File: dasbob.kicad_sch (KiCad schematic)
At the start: 68 parts, among them J1 TRRS LEFT, J2 TRRS LEFT, SW1 SW_Push, SW10 SW_Push, SW11 SW_Push, SW12 SW_Push, SW13 SW_Push, SW14 SW_Push, SW15 SW_Push, SW16 SW_Push, SW17 SW_Push, SW18 SW_Push, SW19 SW_Push, SW2 SW_Push, SW20 SW_Push, SW21 SW_Push, SW22 SW_Push, SW23 SW_Push, SW24 SW_Push, SW25 SW_Push, SW26 SW_Push, SW27 SW_Push, SW28 SW_Push, SW29 SW_Push, SW3 SW_Push, SW30 SW_Push, SW31 SW_Push, SW32 SW_Push, SW33 SW_Push, SW34 SW_Push, SW35 SW_Push, SW36 SW_Push, SW4 SW_Push, SW5 SW_Push, SW6 SW_Push, SW7 SW_Push, SW8 SW_Push, SW9 SW_Push, U1 Elite-C RIGHT, U2 Elite-C LEFT, U3 OLED1, U4 OLED2

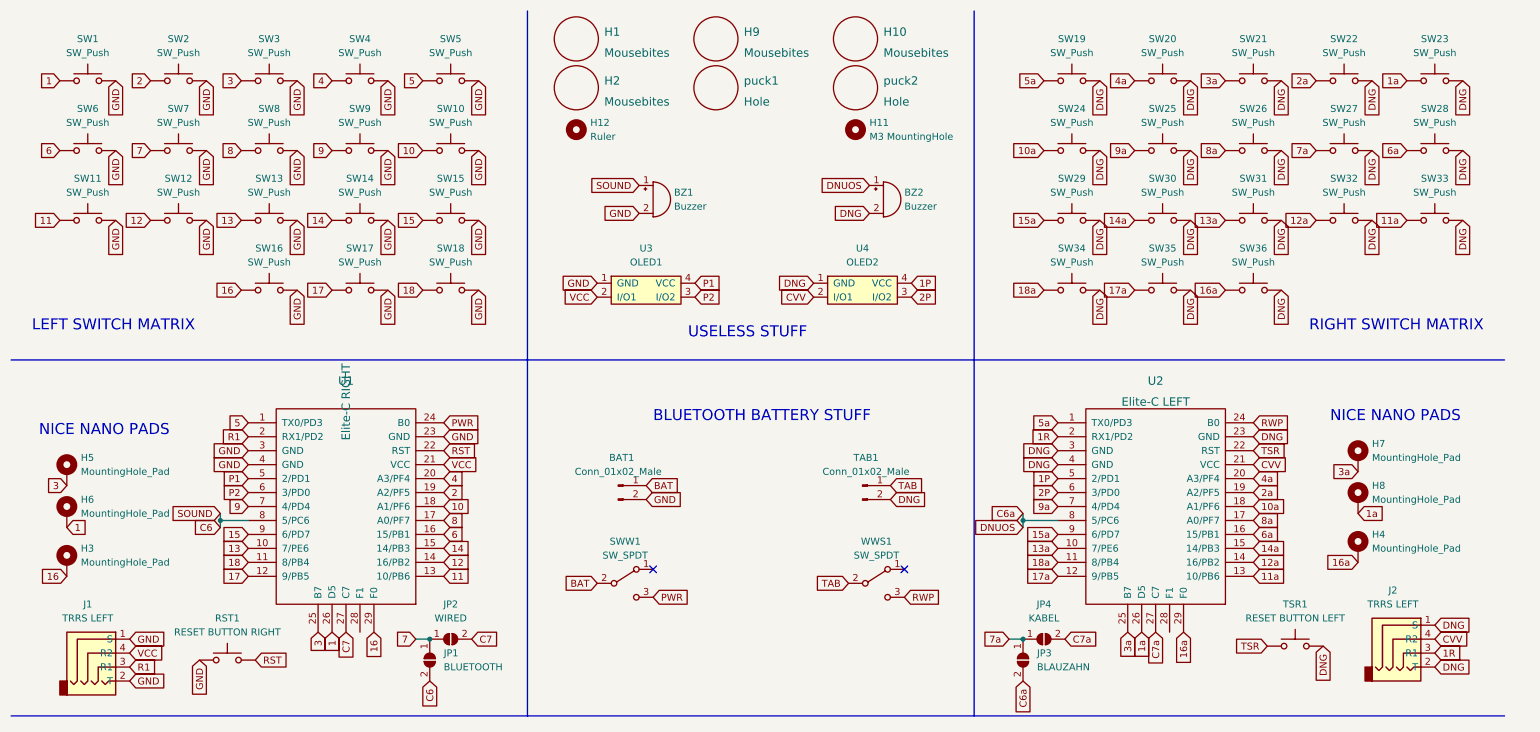
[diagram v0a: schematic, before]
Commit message: Remove jumpers
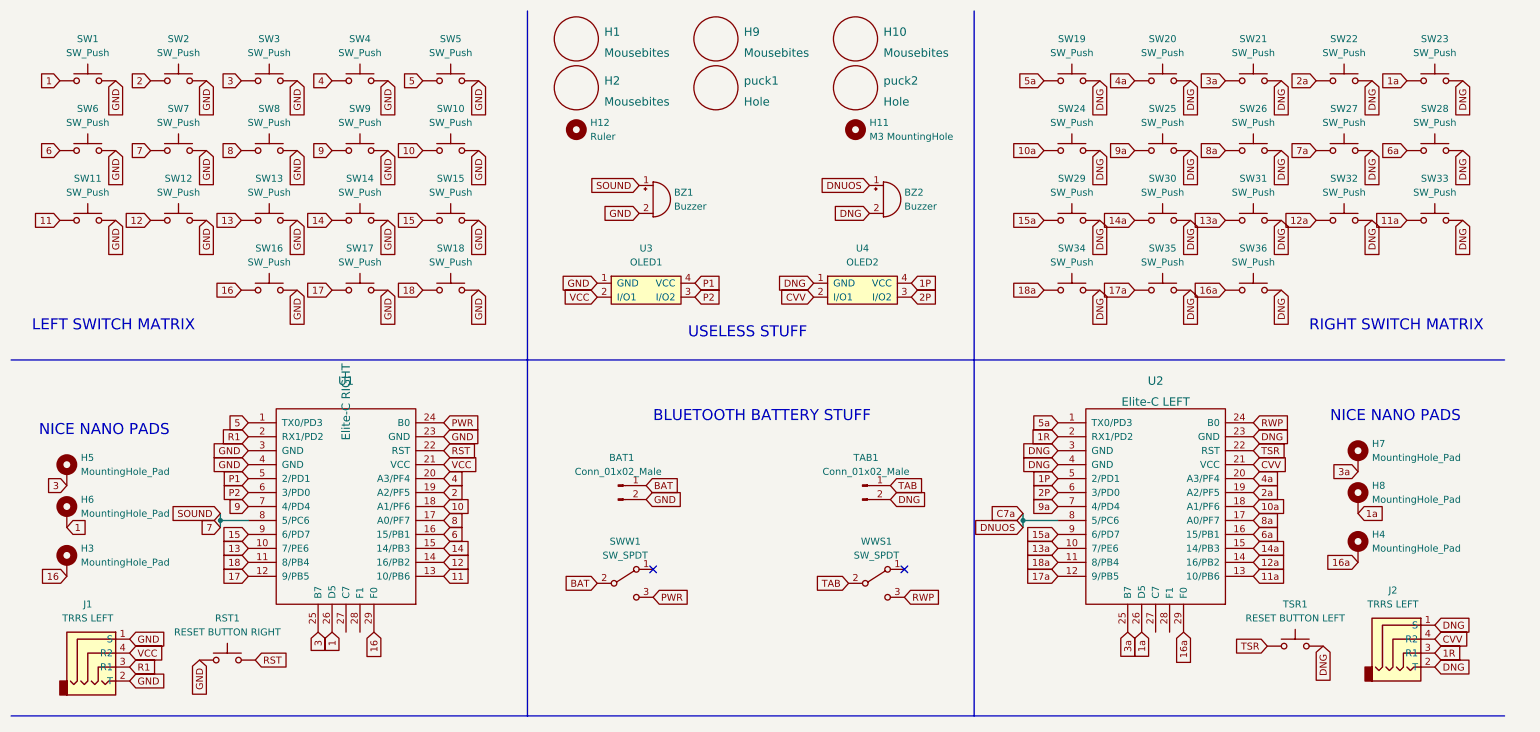
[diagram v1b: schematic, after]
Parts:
- removed JP1: BLUETOOTH, keebio:JUMPER_SMD_2DUB, symbol Jumper:SolderJumper_2_Open
- removed JP2: WIRED, keebio:JUMPER_SMD_2DUB, symbol Jumper:SolderJumper_2_Open
- removed JP3: BLAUZAHN, keebio:JUMPER_SMD_2DUB, symbol Jumper:SolderJumper_2_Open
- removed JP4: KABEL, keebio:JUMPER_SMD_2DUB, symbol Jumper:SolderJumper_2_Open
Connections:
- net C6 is gone; now on net 7: BZ1.1 (-), U1.8 (5/PC6)
- net C6a is gone; now on net C7a: BZ2.1 (-), U2.8 (5/PC6)
- net C7a: no longer U2.27 (C7)
- net C7: no longer names the net of U1.27 (C7)
